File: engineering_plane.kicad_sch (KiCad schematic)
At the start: 3 parts, among them U1 TPS54302DDCR, U2 TPS54302DDCR

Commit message: feat: power section done, onto sensors
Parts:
- added C1, C10, C2, C9: 10u, Capacitor_SMD:C_1206_3216Metric, symbol Device:C
- added C11, C12, C3, C5: 0.1u, Capacitor_SMD:C_0805_2012Metric, symbol Device:C
- added C13, C14, C6, C7: 22u, Capacitor_SMD:C_1206_3216Metric, symbol Device:C
- added C15, C8: 100p, Capacitor_SMD:C_0805_2012Metric, symbol Device:C
- added C4: 100u, Capacitor_SMD:CP_Elec_6.3x7.7, symbol PCM_SparkFun-Capacitor:C_Polarized
- added D1: SMF15A, Diode_SMD:D_SMF, symbol Diode:SMF15A
- added D2: SS24, Diode_SMD:D_SMA, symbol Diode:SS24
- added J1: Conn_01x02_Pin, Connector_AMASS:AMASS_XT30PW-M_1x02_P2.50mm_Horizontal, symbol Connector:Conn_01x02_Pin
- added L1, L2: 10u, Inductor_SMD:L_7.3x7.3_H4.5, symbol Device:L
- added R1, R3: 100k, PCM_SparkFun-Resistor:R_0603_1608Metric, symbol PCM_SparkFun-Resistor:R
- added R2: 13.3k, PCM_SparkFun-Resistor:R_0603_1608Metric, symbol PCM_SparkFun-Resistor:R
- added R4: 11k, PCM_SparkFun-Resistor:R_0603_1608Metric, symbol PCM_SparkFun-Resistor:R
- U1, U2: footprint TPS54302DDCR:SOT95P280X110-6N -> TPS54302:SOT95P280X110-6N
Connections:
- net GND: now reaches U2.1 (GND)
- net GND: now also A1.13 (GND), A1.18 (GND), A1.23 (GND), A1.28 (GND), A1.3 (GND), A1.38 (GND), A1.8 (GND), U1.1 (GND), C1.2, C10.2, C11.2, C13.2, C14.2, C2.2, C3.2, C4.2, C6.2, C7.2, C9.2, D1.2 (A2), J1.1 (Pin_1), R2.1, R4.1
- net at U2.2 (SW): now also C12.2, L2.1
- net VBATT: now reaches U2.3 (VIN)
- net VBATT: now also U1.3 (VIN), C1.1, C10.1, C11.1, C2.1, C3.1, C4.1, C9.1, D1.1 (A1), J1.2 (Pin_2)
- net 6v_div: now reaches U2.4 (FB)
- net 6v_div: now also C15.2, R3.1, R4.2
- net at U2.6 (BOOT): now also C12.1
- net +3V3: now reaches A1.36 (3V3)
- net at A1.39 (VSYS): now also D2.1 (K)
- net at U1.2 (SW): now also C5.2, L1.1
- net 5v_div: now reaches U1.4 (FB)
- net 5v_div: now also C8.2, R1.1, R2.2
- net at U1.6 (BOOT): now also C5.1
- new net +5V: C6.1, C7.1, C8.1, D2.2 (A), L1.2, R1.2
- new net +6V: C13.1, C14.1, C15.1, L2.2, R3.2
- no-connect marks 0 -> 2
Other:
- note added: "5.08V [4.99V ... 5.17V]"
- note added: "6.01V [5.91V ... 6.12V]"
- note added: "Battery Connector"
- moved on the sheet: A1, U1, U2

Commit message: feat: schematic mostly finished, onto the PCB
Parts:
- added C11: 100n, Capacitor_SMD:C_0603_1608Metric, symbol Device:C
- added C15, C16: 1u, Capacitor_SMD:C_0603_1608Metric, symbol Device:C
- added C4: 470u, Capacitor_SMD:CP_Elec_10x10.5, symbol PCM_SparkFun-Capacitor:C_Polarized
- added C7, C9: 10u, Capacitor_SMD:C_1206_3216Metric, symbol Device:C
- added D2: SMF6V5A, Diode_SMD:D_SMF, symbol Diode:SMF6V5A
- added IC1: LP5907MFX-3.3_NOPB, eng_plane_lib:SOT95P280X145-5M, symbol eng_plane_lib:LP5907MFX-3.3_NOPB
- added J1, J2: Conn_01x01_Pin, Connector_Wire:SolderWire-2sqmm_1x01_D2mm_OD3.9mm, symbol Connector:Conn_01x01_Pin
- added J3, J4, J6: JST_1mm_4, PCM_SparkFun-Connector:JST_1x04_P1.0mm_Horizontal_SMD, symbol PCM_SparkFun-Connector:Conn_01x04_JST_P1.0mm_Horizontal_SMD
- added R3: 47k, PCM_SparkFun-Resistor:R_0603_1608Metric, symbol PCM_SparkFun-Resistor:R
- added R4: 1k, PCM_SparkFun-Resistor:R_0603_1608Metric, symbol PCM_SparkFun-Resistor:R
- added R5, R6, R7, R8: 100, PCM_SparkFun-Resistor:R_0603_1608Metric, symbol PCM_SparkFun-Resistor:R
- A1: footprint Module:RaspberryPi_Pico_W_SMD_HandSolder -> Module:RaspberryPi_Pico_Common_SMD
- U1, U2: symbol TPS54302DDCR:TPS54302DDCR -> eng_plane_lib:TPS54302DDCR
- renumbered C8 to C10, C9 to C12, C10 to C13, C11 to C14, C12 to C17, C13 to C18, C14 to C19, C4 to C20, C15 to C21, C7 to C8, D2 to D1, D1 to D3, J1 to J5, R4 to R10, R3 to R9
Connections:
- net +3V3: now also C16.1, IC1.5 (OUT), J3.1; no longer A1.36 (3V3)
- net +5V: now also C15.1, IC1.1 (IN), IC1.3 (EN), J4.1, J6.2
- net +6V: now also C4.1, C7.1, C9.1, D2.1 (A1)
- net GND: now also C11.1, C15.2, C16.2, C4.2, C7.2, C9.2, D2.2 (A2), IC1.2 (GND), J2.1 (Pin_1), J3.4, J4.4, J6.1, R4.2
- net VBATT: now also J1.1 (Pin_1), R3.1
- new net: J6.4, R8.1
- new net: J3.3, R6.1
- new net: J6.3, R7.1
- new net: J3.2, R5.1
- new net adc_v: C11.2, R3.2, R4.1
- new net gps_rx: R5.2
- new net gps_tx: R6.2
- new net pitot_scl: J4.2
- new net pitot_sda: J4.3
- new net rc_rx: R7.2
- new net rc_tx: R8.2
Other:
- added sheet bmi270 (bmi270.kicad_sch)
- added sheet bmp390 (bmp390.kicad_sch)
- added sheet servos (servos.kicad_sch)
- note added: "3V3 LDO"
- note added: "6DoF IMU"
- note added: "ADC voltage 0.1754 x VBATT"
- note added: "Barometer"
- note added: "DiffPressure Sensor"
- note added: "ESC connection"
- note added: "ExpressLRS module BETAFPV Nano RX"
- note added: "GPS module"
- note added: "I2C adrr: 0x68 I2C speed: max 1MHz"
- note added: "I2C adrr: 0x76 I2C speed: max 1MHz"
- note added: "Servos subsystem"
- moved on the sheet: A1, D1

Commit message: sisyphus goes hard, awaiting review.
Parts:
- added H1, H2, H3, H4: MountingHole_Pad, MountingHole:MountingHole_3.2mm_M3_Pad, symbol Mechanical:MountingHole_Pad
- added J1: JST_1mm_4, PCM_SparkFun-Connector:JST_1x04_P1.0mm_Horizontal_SMD, symbol PCM_SparkFun-Connector:Conn_01x04_JST_P1.0mm_Horizontal_SMD
- added J12: Conn_01x07_Pin, Connector_PinHeader_2.54mm:PinHeader_1x07_P2.54mm_Vertical, symbol Connector:Conn_01x07_Pin
- added J14: Conn_01x04_Pin, Connector_PinHeader_2.54mm:PinHeader_1x04_P2.54mm_Vertical, symbol Connector:Conn_01x04_Pin
- added J15: Conn_01x03, eng_plane_lib:1718564003, symbol Connector_Generic:Conn_01x03
- added R1, R2, R21, R22: 4.7k, PCM_SparkFun-Resistor:R_0603_1608Metric, symbol PCM_SparkFun-Resistor:R
- added R23: 100, PCM_SparkFun-Resistor:R_0603_1608Metric, symbol PCM_SparkFun-Resistor:R
- added R24: 10k, PCM_SparkFun-Resistor:R_0603_1608Metric, symbol PCM_SparkFun-Resistor:R
- C10, C14, C17, C3, C5: footprint Capacitor_SMD:C_0805_2012Metric -> Capacitor_SMD:C_0603_1608Metric
- R6: renamed from R4; value 1k -> 10k
- U1, U2: footprint TPS54302:SOT95P280X110-6N -> eng_plane_lib:SOT95P280X110-6N
- renumbered J1 to J2, J2 to J3, J3 to J4, J4 to J5, J5 to J6, J6 to J7, R8 to R10, R9 to R11, R10 to R12, R1 to R3, R2 to R4, R3 to R5, R5 to R7, R6 to R8, R7 to R9
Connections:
- net pitot_scl is gone; now on net i2c1_scl: J5.2
- net pitot_sda is gone; now on net i2c1_sda: J5.3
- net +3V3: now also J1.1, J12.6 (Pin_6), J14.3 (Pin_3), R1.1, R2.1, R21.1, R22.1
- net GND: now also H1.1, H2.1, H3.1, H4.1, J1.4, J12.7 (Pin_7), J14.4 (Pin_4), J15.1 (Pin_1), R24.1
- net adc_v: now also A1.32 (GPIO27_ADC1)
- net gps_rx: now also A1.6 (GPIO4)
- net gps_tx: now also A1.7 (GPIO5)
- net rc_rx: now also A1.1 (GPIO0)
- net rc_tx: now also A1.2 (GPIO1)
- net i2c1_scl: now reaches A1.10 (GPIO7)
- net i2c1_scl: now also J1.2, R22.2
- net at A1.11 (GPIO8): now also J12.1 (Pin_1)
- net at A1.12 (GPIO9): now also J12.2 (Pin_2)
- net at A1.14 (GPIO10): now also J12.3 (Pin_3)
- net at A1.15 (GPIO11): now also J12.4 (Pin_4)
- net at A1.16 (GPIO12): now also J12.5 (Pin_5)
- net mmc_int: now reaches A1.17 (GPIO13)
- net pwm0_a: now reaches A1.21 (GPIO16)
- net pwm0_b: now reaches A1.22 (GPIO17)
- net pwm1_a: now reaches A1.24 (GPIO18)
- net pwm1_a: now also R23.1
- net bmp_int: now reaches A1.25 (GPIO19)
- net i2c0_sda: now reaches A1.26 (GPIO20)
- net i2c0_sda: now also R1.2
- net i2c0_scl: now reaches A1.27 (GPIO21)
- net i2c0_scl: now also R2.2
- net bmi_int: now reaches A1.29 (GPIO22)
- net pwm5_a: now reaches A1.31 (GPIO26_ADC0)
- net pwm6_a: now reaches A1.34 (GPIO28_ADC2)
- net at A1.4 (GPIO2): now also J14.1 (Pin_1)
- net at A1.5 (GPIO3): now also J14.2 (Pin_2)
- net i2c1_sda: now reaches A1.9 (GPIO6)
- net i2c1_sda: now also J1.3, R21.2
- new net: J15.3 (Pin_3), R23.2, R24.2
- no-connect marks 2 -> 9
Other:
- added sheet mmc (mmc.kicad_sch)
- note added: "Backup_Mag"
- note added: "Montaż"
- note added: "Onboard Magnetometr"
- note added: "unused gpio connector"
- moved on the sheet: A1, C7, D1, J2, J3

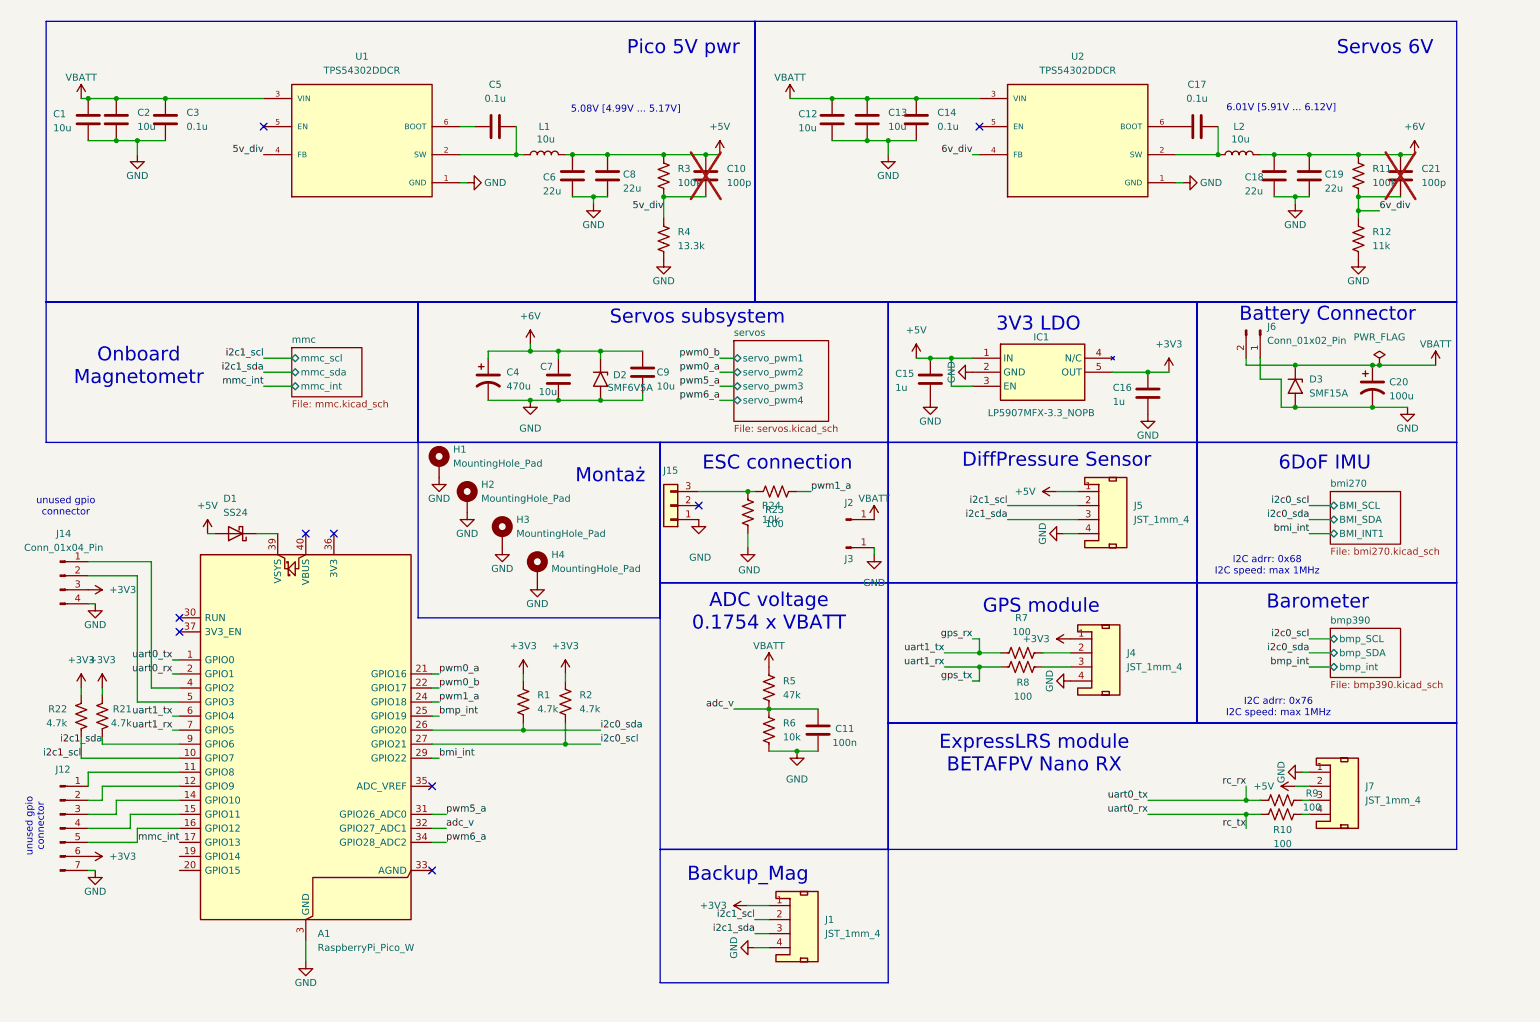
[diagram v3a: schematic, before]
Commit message: feat: rev1 added sdcard
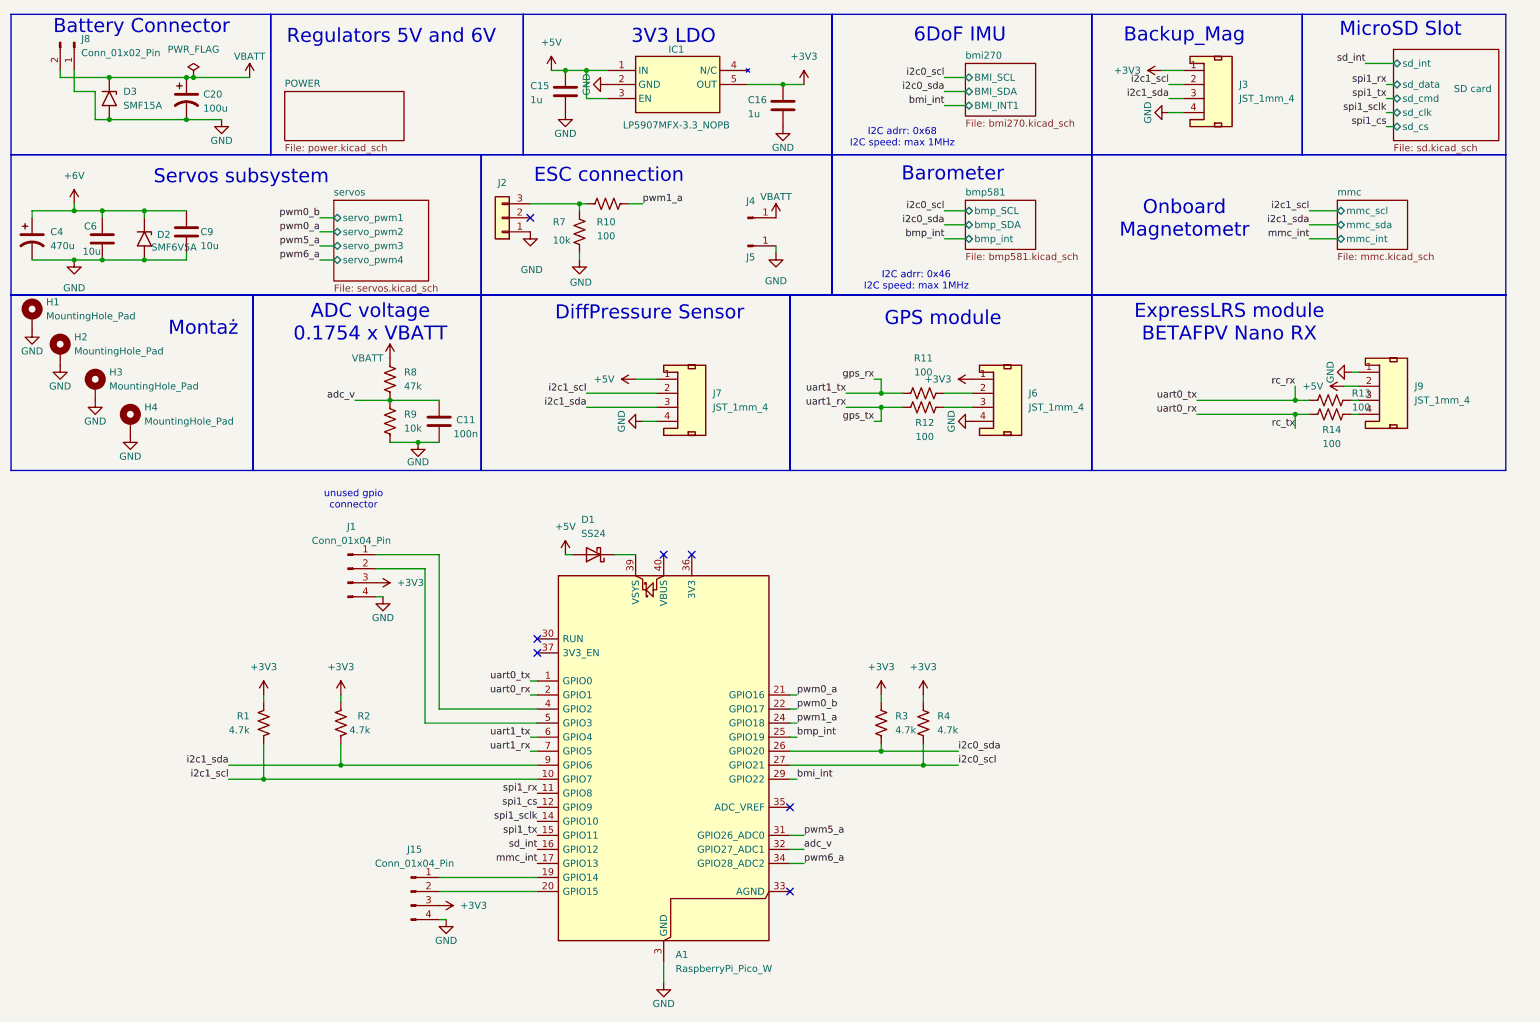
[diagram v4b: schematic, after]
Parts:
- removed C1, C12, C13, C2, C7: 10u, Capacitor_SMD:C_1206_3216Metric, symbol Device:C
- removed C10: 100p, Capacitor_SMD:C_0603_1608Metric, symbol Device:C
- removed C14, C17, C3, C5: 0.1u, Capacitor_SMD:C_0603_1608Metric, symbol Device:C
- removed C18, C19, C8: 22u, Capacitor_SMD:C_1206_3216Metric, symbol Device:C
- removed C21: 100p, Capacitor_SMD:C_0805_2012Metric, symbol Device:C
- removed J1, J4, J5: JST_1mm_4, PCM_SparkFun-Connector:JST_1x04_P1.0mm_Horizontal_SMD, symbol PCM_SparkFun-Connector:Conn_01x04_JST_P1.0mm_Horizontal_SMD
- removed J12: Conn_01x07_Pin, Connector_PinHeader_2.54mm:PinHeader_1x07_P2.54mm_Vertical, symbol Connector:Conn_01x07_Pin
- removed J15: Conn_01x03, eng_plane_lib:1718564003, symbol Connector_Generic:Conn_01x03
- removed J2, J3: Conn_01x01_Pin, Connector_Wire:SolderWire-2sqmm_1x01_D2mm_OD3.9mm, symbol Connector:Conn_01x01_Pin
- removed J6: Conn_01x02_Pin, Connector_AMASS:AMASS_XT30PW-M_1x02_P2.50mm_Horizontal, symbol Connector:Conn_01x02_Pin
- removed L1, L2: 10u, Inductor_SMD:L_7.3x7.3_H4.5, symbol Device:L
- removed R23: 100, PCM_SparkFun-Resistor:R_0603_1608Metric, symbol PCM_SparkFun-Resistor:R
- removed R24, R6: 10k, PCM_SparkFun-Resistor:R_0603_1608Metric, symbol PCM_SparkFun-Resistor:R
- removed R3: 100k, PCM_SparkFun-Resistor:R_0603_1608Metric, symbol PCM_SparkFun-Resistor:R
- removed R4: 13.3k, PCM_SparkFun-Resistor:R_0603_1608Metric, symbol PCM_SparkFun-Resistor:R
- removed R5: 47k, PCM_SparkFun-Resistor:R_0603_1608Metric, symbol PCM_SparkFun-Resistor:R
- removed U1, U2: TPS54302DDCR, eng_plane_lib:SOT95P280X110-6N, symbol eng_plane_lib:TPS54302DDCR
- added J15: Conn_01x04_Pin, Connector_PinHeader_2.54mm:PinHeader_1x04_P2.54mm_Vertical, symbol Connector:Conn_01x04_Pin
- added J2: Conn_01x03, eng_plane_lib:1718564003, symbol Connector_Generic:Conn_01x03
- added J3, J6, J9: JST_1mm_4, PCM_SparkFun-Connector:JST_1x04_P1.0mm_Horizontal_SMD, symbol PCM_SparkFun-Connector:Conn_01x04_JST_P1.0mm_Horizontal_SMD
- added J4, J5: Conn_01x01_Pin, Connector_Wire:SolderWire-2sqmm_1x01_D2mm_OD3.9mm, symbol Connector:Conn_01x01_Pin
- added J8: Conn_01x02_Pin, Connector_AMASS:AMASS_XT30PW-M_1x02_P2.50mm_Horizontal, symbol Connector:Conn_01x02_Pin
- added R13, R14: 100, PCM_SparkFun-Resistor:R_0603_1608Metric, symbol PCM_SparkFun-Resistor:R
- C6: value 22u -> 10u
- R11: value 100k -> 100
- R12: value 11k -> 100
- R7, R9: value 100 -> 10k
- R8: value 100 -> 47k
- renumbered J14 to J1, R22 to R1, R21 to R2, R1 to R3, R2 to R4
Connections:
- net +3V3: now also J15.3 (Pin_3), J3.1, J6.1
- net +5V: now also J7.1, J9.2; no longer C6.1, J7.2
- net +6V: now also C6.1; no longer R11.2
- net GND: now also J7.4, R7.1, R9.2, J15.4 (Pin_4), J2.1 (Pin_1), J3.4, J5.1 (Pin_1), J6.4, J8.1 (Pin_1), J9.1; no longer J7.1, R12.1
- net VBATT: now also R8.1, J4.1 (Pin_1), J8.2 (Pin_2)
- net adc_v: now also R8.2, R9.1
- net gps_rx: now also R11.2; no longer R7.2
- net gps_tx: now also R12.2; no longer R8.2
- net i2c1_scl: now also J7.2, J3.2
- net i2c1_sda: now also J7.3, J3.3
- net pwm1_a: now also R10.1
- net rc_rx: now also R13.2; no longer R9.2
- net rc_tx: now also R14.2; no longer R10.2
- net spi1_rx: now reaches A1.11 (GPIO8)
- net spi1_cs: now reaches A1.12 (GPIO9)
- net spi1_sclk: now reaches A1.14 (GPIO10)
- net spi1_tx: now reaches A1.15 (GPIO11)
- net sd_int: now reaches A1.16 (GPIO12)
- net at A1.19 (GPIO14): now also J15.1 (Pin_1)
- net at A1.20 (GPIO15): now also J15.2 (Pin_2)
- net 6v_div: no longer names the net of R11.1
- net 6v_div: now also J6.2; no longer R12.2
- new net: J6.3, R12.1
- new net: J9.3, R13.1
- new net: J9.4, R14.1
- new net: J2.3 (Pin_3), R10.2, R7.2
- no-connect marks 9 -> 7
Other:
- removed sheet bmp390
- added sheet POWER (power.kicad_sch)
- added sheet SD card (sd.kicad_sch)
- added sheet bmp581 (bmp581.kicad_sch)
- note added: "I2C adrr: 0x46 I2C speed: max 1MHz"
- note added: "MicroSD Slot"
- note added: "Regulators 5V and 6V"
- note removed: "5.08V [4.99V ... 5.17V]"
- note removed: "6.01V [5.91V ... 6.12V]"
- note removed: "I2C adrr: 0x76 I2C speed: max 1MHz"
- note removed: "Pico 5V pwr"
- note removed: "Servos 6V"
- moved on the sheet: A1, D1, J1, R1, R2, R3, R4

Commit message: feat: final changes, sent to prod
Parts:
- D3: renamed from D1; footprint Diode_SMD:D_SMA -> Diode_SMD:D_SMA-SMB_Universal_Handsoldering
- R11: renamed from R13; value 100 -> 22
- R12: renamed from R14; value 100 -> 22
- R6: renamed from R10; value 100 -> 22
- R8: renamed from R11; value 100 -> 22
- R9: renamed from R12; value 100 -> 22
- renumbered C4 to C1, C6 to C2, C20 to C3, C9 to C4, C11 to C5, C15 to C6, C16 to C7, D3 to D1, J8 to J1, J9 to J10, J1 to J2, J15 to J3, J2 to J4, J7 to J5, J4 to J6, J5 to J7, J6 to J8, J3 to J9, R4 to R10, R8 to R3, R9 to R4, R7 to R5, R3 to R7
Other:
- note added: "Montage"
- note removed: "Montaż"
- company: (none) -> Politechnika Wrocławska, W12N
- title: (none) -> PCB-Monoplane
- moved on the sheet: D3, J2, R11, R12, R2

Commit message: Revised componenents, need to route
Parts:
- removed A1: RaspberryPi_Pico_W, Module:RaspberryPi_Pico_Common_SMD, symbol MCU_Module:RaspberryPi_Pico_W
- removed C2, C4: 10u, Capacitor_SMD:C_1206_3216Metric, symbol Device:C
- removed C5: 100n, Capacitor_SMD:C_0603_1608Metric, symbol Device:C
- removed C6, C7: 1u, Capacitor_SMD:C_0603_1608Metric, symbol Device:C
- removed D1: SMF15A, Diode_SMD:D_SMF, symbol Diode:SMF15A
- removed D2: SMF6V5A, Diode_SMD:D_SMF, symbol Diode:SMF6V5A
- removed D3: SS24, Diode_SMD:D_SMA-SMB_Universal_Handsoldering, symbol Diode:SS24
- removed H4: MountingHole_Pad, MountingHole:MountingHole_3.2mm_M3_Pad, symbol Mechanical:MountingHole_Pad
- removed IC1: LP5907MFX-3.3_NOPB, eng_plane_lib:SOT95P280X145-5M, symbol eng_plane_lib:LP5907MFX-3.3_NOPB
- removed J10, J5, J8, J9: JST_1mm_4, PCM_SparkFun-Connector:JST_1x04_P1.0mm_Horizontal_SMD, symbol PCM_SparkFun-Connector:Conn_01x04_JST_P1.0mm_Horizontal_SMD
- removed J2, J3: Conn_01x04_Pin, Connector_PinHeader_2.54mm:PinHeader_1x04_P2.54mm_Vertical, symbol Connector:Conn_01x04_Pin
- removed J4: Conn_01x03, eng_plane_lib:1718564003, symbol Connector_Generic:Conn_01x03
- removed J6, J7: Conn_01x01_Pin, Connector_Wire:SolderWire-2sqmm_1x01_D2mm_OD3.9mm, symbol Connector:Conn_01x01_Pin
- removed R1, R10, R2, R7: 4.7k, PCM_SparkFun-Resistor:R_0603_1608Metric, symbol PCM_SparkFun-Resistor:R
- removed R11, R12, R6, R8, R9: 22, PCM_SparkFun-Resistor:R_0603_1608Metric, symbol PCM_SparkFun-Resistor:R
- removed R3: 47k, PCM_SparkFun-Resistor:R_0603_1608Metric, symbol PCM_SparkFun-Resistor:R
- removed R4, R5: 10k, PCM_SparkFun-Resistor:R_0603_1608Metric, symbol PCM_SparkFun-Resistor:R
- added C102: 100nF, PCM_JLCPCB:C_0402, symbol PCM_JLCPCB-Capacitors:0402,100nF,(2)
- added C104, C105: 10uF, PCM_JLCPCB:C_1206, symbol PCM_JLCPCB-Capacitors:1206,10uF
- added D101: SMF15A, PCM_JLCPCB:D_SOD-123FL, symbol PCM_JLCPCB-Diodes:TVS-Uni,SMF15A
- added D102: SMF6.5A, PCM_JLCPCB:D_SOD-123FL, symbol PCM_JLCPCB-Diodes:TVS-Uni,SMF6.5A
- added H102, H103, H104: (no value), PCM_JLCPCB:Hole_Tooling_JLCPCB, symbol PCM_JLCPCB-Manufacturing:Tooling Hole, PCM_JLCPCB, 1.152mm
- added J102, J103: Conn_01x01_Pin, Connector_Wire:SolderWire-2sqmm_1x01_D2mm_OD3.9mm, symbol Connector:Conn_01x01_Pin
- added R101: 47kΩ, PCM_JLCPCB:R_0402, symbol PCM_JLCPCB-Resistors:0402,47kΩ
- added R102: 10kΩ, PCM_JLCPCB:R_0402, symbol PCM_JLCPCB-Resistors:0402,10kΩ
- renumbered C3 to C101, C1 to C103, H1 to H101, H2 to H105, H3 to H106, J1 to J101
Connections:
- net +6V: now also C104.1, C105.1, D102.1
- net GND: now also C102.2, C104.2, C105.2, D101.2, D102.2, R102.2
- net VBATT: now also D101.1, J102.1 (Pin_1), R101.1
- new net MCU/adc_v: C102.1, R101.2, R102.1
- no-connect marks 7 -> 0
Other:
- added sheet BackupMag (BackupMag.kicad_sch)
- added sheet DiffPressure (DiffPressure.kicad_sch)
- added sheet ESC (ESC.kicad_sch)
- added sheet GPS (GPS.kicad_sch)
- added sheet MCU (MCU.kicad_sch)
- added sheet RC_ctl (RC_ctl.kicad_sch)
- sheet SD card ports: added SPI4{SPI4}; removed sd_clk, sd_cmd, sd_data
- sheet bmi270 ports: added I2C{I2C}; removed BMI_SCL, BMI_SDA
- sheet bmp581 ports: added I2C{I2C}; removed bmp_SCL, bmp_SDA
- sheet mmc ports: added I2C{I2C}; removed mmc_scl, mmc_sda
- note added: "0.1754 x VBATT"
- note added: "ESC Power"
- note added: "Montage & Assembly"
- note added: "Regulators 5V and 6V 3v3 LDO"
- note added: "Tooling Holes"
- note removed: "3V3 LDO"
- note removed: "6DoF IMU"
- note removed: "ADC voltage 0.1754 x VBATT"
- note removed: "Backup_Mag"
- note removed: "Barometer"
- note removed: "DiffPressure Sensor"
- note removed: "ESC connection"
- note removed: "ExpressLRS module BETAFPV Nano RX"
- note removed: "GPS module"
- note removed: "MicroSD Slot"
- note removed: "Montage"
- note removed: "Onboard Magnetometr"
- note removed: "Regulators 5V and 6V"
- note removed: "unused gpio connector"
- moved on the sheet: C101, C103, H101, H105, H106, J101

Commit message: finished routing
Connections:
- net GND: now also J103.1 (Pin_1)
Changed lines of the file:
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@@
+		)
+	)
+	(wire
+		(pts
+			(xy 267.97 153.67) (xy 267.97 154.94)
+		)
+		(stroke
+			(width 0)
+			(type default)
 		)
 	)
